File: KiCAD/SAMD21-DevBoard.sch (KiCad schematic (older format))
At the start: 22 parts, among them J1 .1\" Headers, J2 .1\" Headers, J3 Cortex_Debug, SW1 B3FS-4005P, U1 SAMD21G18A-AU, Y1 32.768KHz

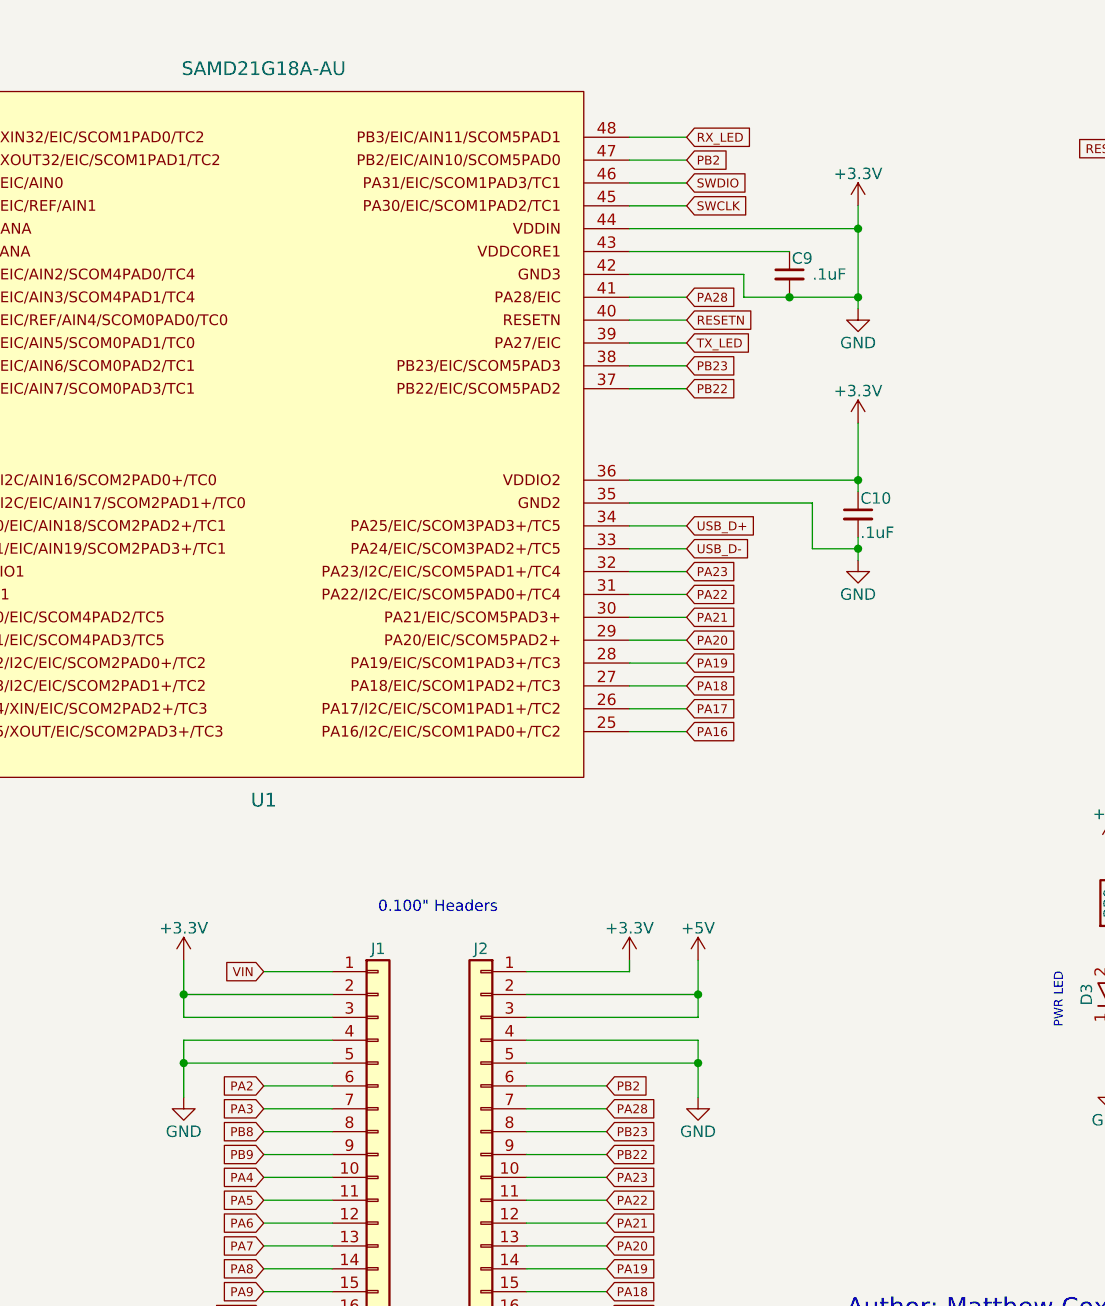
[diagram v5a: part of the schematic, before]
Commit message: Board layout and fixing schematic errors
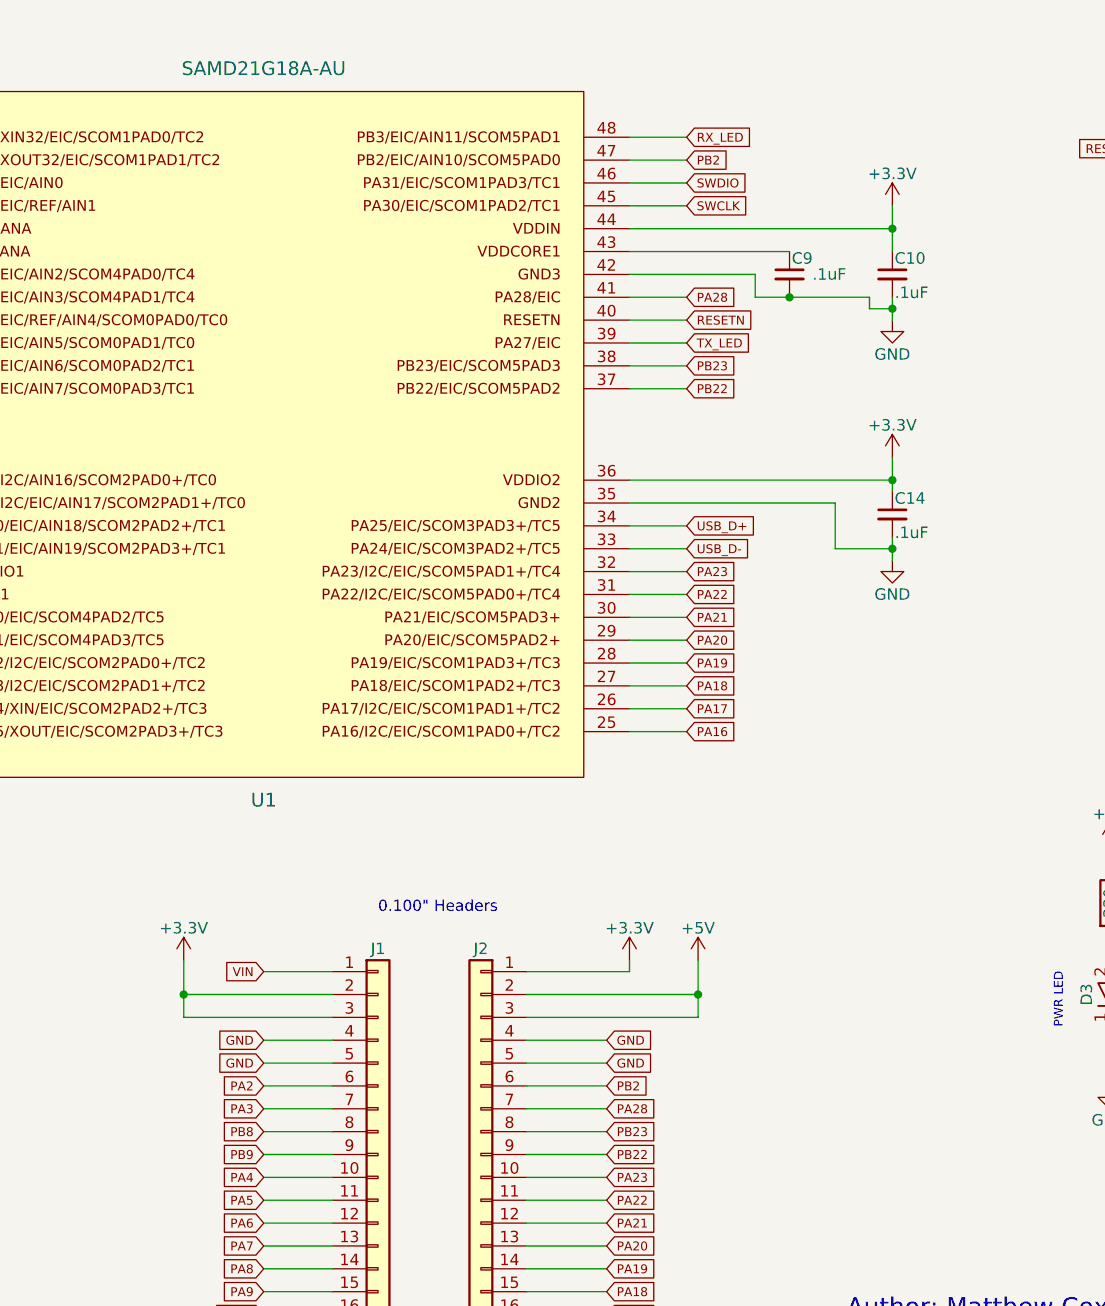
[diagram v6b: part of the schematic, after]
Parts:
- added C14: .1uF, symbol C_Small
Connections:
- net +3V3: now also C14.1; no longer C10.2, C11.2, C12.2, C13.2, C7.1, C8.1, C9.2, D3.1 (K), D4.1 (GND), J1.4 (Pin_4), J1.5 (Pin_5), J2.4 (Pin_4), J2.5 (Pin_5), J3.3 (GND), J3.5 (GND), SW1.3, SW1.4, U1.18, U1.35, U1.42, U1.5
- new net GND: C10.2, C11.2, C12.2, C13.2, C14.2, C7.1, C8.1, C9.2, D3.1 (K), D4.1 (GND), J1.4 (Pin_4), J1.5 (Pin_5), J2.4 (Pin_4), J2.5 (Pin_5), J3.3 (GND), J3.5 (GND), SW1.3, SW1.4, U1.18, U1.35, U1.42, U1.5
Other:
- moved on the sheet: C10
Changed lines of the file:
@@
 L +3.3V #PWR04
 U 1 1 5BF30FCE
-P 7100 2100
-F 0 "#PWR04" H 7100 1950 50  0001 C CNN
-F 1 "+3.3V" H 7100 2240 50  0000 C CNN
-F 2 "" H 7100 2100 50  0001 C CNN
-F 3 "" H 7100 2100 50  0001 C CNN
-	1    7100 2100
-	1    0    0    -1
-$EndComp
-$Comp
-L GND #PWR05
-U 1 1 5BF30FEC
-P 7100 2550
-F 0 "#PWR05" H 7100 2300 50  0001 C CNN
-F 1 "GND" H 7100 2400 50  0000 C CNN
-F 2 "" H 7100 2550 50  0001 C CNN
-F 3 "" H 7100 2550 50  0001 C CNN
-	1    7100 2550
+P 7250 2100
+F 0 "#PWR04" H 7250 1950 50  0001 C CNN
+F 1 "+3.3V" H 7250 2240 50  0000 C CNN
+F 2 "" H 7250 2100 50  0001 C CNN
+F 3 "" H 7250 2100 50  0001 C CNN
+	1    7250 2100
 	1    0    0    -1
 $EndComp
@@
 $EndComp
 $Comp
-L +3.3V #PWR06
+L +3.3V #PWR05
 U 1 1 5BF31404
 P 1900 3450
-F 0 "#PWR06" H 1900 3300 50  0001 C CNN
+F 0 "#PWR05" H 1900 3300 50  0001 C CNN
 F 1 "+3.3V" H 1900 3590 50  0000 C CNN
 F 2 "" H 1900 3450 50  0001 C CNN
@@
 $EndComp
 $Comp
-L GND #PWR07
+L GND #PWR06
 U 1 1 5BF3142B
 P 1900 4050
-F 0 "#PWR07" H 1900 3800 50  0001 C CNN
+F 0 "#PWR06" H 1900 3800 50  0001 C CNN
 F 1 "GND" H 1900 3900 50  0000 C CNN
 F 2 "" H 1900 4050 50  0001 C CNN
@@
 $EndComp
 $Comp
-L +3.3V #PWR08
-U 1 1 5BF318C5
-P 7100 3050
-F 0 "#PWR08" H 7100 2900 50  0001 C CNN
-F 1 "+3.3V" H 7100 3190 50  0000 C CNN
-F 2 "" H 7100 3050 50  0001 C CNN
-F 3 "" H 7100 3050 50  0001 C CNN
-	1    7100 3050
-	1    0    0    -1
-$EndComp
-$Comp
-L GND #PWR09
+L GND #PWR07
 U 1 1 5BF318CB
-P 7100 3650
-F 0 "#PWR09" H 7100 3400 50  0001 C CNN
-F 1 "GND" H 7100 3500 50  0000 C CNN
-F 2 "" H 7100 3650 50  0001 C CNN
-F 3 "" H 7100 3650 50  0001 C CNN
-	1    7100 3650
+P 7250 3650
+F 0 "#PWR07" H 7250 3400 50  0001 C CNN
+F 1 "GND" H 7250 3500 50  0000 C CNN
+F 2 "" H 7250 3650 50  0001 C CNN
+F 3 "" H 7250 3650 50  0001 C CNN
+	1    7250 3650
 	1    0    0    -1
 $EndComp
@@
 L C_Small C10
 U 1 1 5BF318D3
-P 7100 3450
-F 0 "C10" H 7110 3520 50  0000 L CNN
-F 1 ".1uF" H 7110 3370 50  0000 L CNN
-F 2 "Capacitors_SMD:C_1206" H 7100 3450 50  0001 C CNN
-F 3 "" H 7100 3450 50  0001 C CNN
-	1    7100 3450
-	1    0    0    -1
-$EndComp
-$Comp
-L GND #PWR010
+P 7250 2400
+F 0 "C10" H 7260 2470 50  0000 L CNN
+F 1 ".1uF" H 7260 2320 50  0000 L CNN
+F 2 "Capacitors_SMD:C_1206" H 7250 2400 50  0001 C CNN
+F 3 "" H 7250 2400 50  0001 C CNN
+	1    7250 2400
+	1    0    0    -1
+$EndComp
+$Comp
+L GND #PWR08
 U 1 1 5BF31BBB
 P 1850 2750
-F 0 "#PWR010" H 1850 2500 50  0001 C CNN
+F 0 "#PWR08" H 1850 2500 50  0001 C CNN
 F 1 "GND" H 1850 2600 50  0000 C CNN
 F 2 "" H 1850 2750 50  0001 C CNN
@@
 $EndComp
 $Comp
-L +3.3V #PWR011
+L +3.3V #PWR09
 U 1 1 5BF31D4F
 P 1850 1950
-F 0 "#PWR011" H 1850 1800 50  0001 C CNN
+F 0 "#PWR09" H 1850 1800 50  0001 C CNN
 F 1 "+3.3V" H 1850 2090 50  0000 C CNN
 F 2 "" H 1850 1950 50  0001 C CNN
@@
 $EndComp
 $Comp
-L GND #PWR012
+L GND #PWR010
 U 1 1 5BF320EF
 P 2250 2450
-F 0 "#PWR012" H 2250 2200 50  0001 C CNN
+F 0 "#PWR010" H 2250 2200 50  0001 C CNN
 F 1 "GND" H 2250 2300 50  0000 C CNN
 F 2 "" H 2250 2450 50  0001 C CNN
@@
 RESETN
 $Comp
-L +3.3V #PWR013
+L +3.3V #PWR011
 U 1 1 5BF3264F
 P 8550 1400
-F 0 "#PWR013" H 8550 1250 50  0001 C CNN
+F 0 "#PWR011" H 8550 1250 50  0001 C CNN
 F 1 "+3.3V" H 8550 1540 50  0000 C CNN
 F 2 "" H 8550 1400 50  0001 C CNN
@@
 $EndComp
 $Comp
-L GND #PWR014
+L GND #PWR012
 U 1 1 5BF32677
 P 9400 2050
-F 0 "#PWR014" H 9400 1800 50  0001 C CNN
+F 0 "#PWR012" H 9400 1800 50  0001 C CNN
 F 1 "GND" H 9400 1900 50  0000 C CNN
 F 2 "" H 9400 2050 50  0001 C CNN
@@
 RESETN
 $Comp
-L +3.3V #PWR015
+L +3.3V #PWR013
 U 1 1 5BF9AAD9
 P 1400 5900
-F 0 "#PWR015" H 1400 5750 50  0001 C CNN
+F 0 "#PWR013" H 1400 5750 50  0001 C CNN
 F 1 "+3.3V" H 1400 6040 50  0000 C CNN
 F 2 "" H 1400 5900 50  0001 C CNN
@@
 $EndComp
 $Comp
-L GND #PWR016
+L GND #PWR014
 U 1 1 5BF9AB6E
 P 1400 6550
-F 0 "#PWR016" H 1400 6300 50  0001 C CNN
+F 0 "#PWR014" H 1400 6300 50  0001 C CNN
 F 1 "GND" H 1400 6400 50  0000 C CNN
 F 2 "" H 1400 6550 50  0001 C CNN
@@
 PA28
 $Comp
-L +3.3V #PWR017
+L +3.3V #PWR015
 U 1 1 5BF9D0E0
 P 4150 5400
-F 0 "#PWR017" H 4150 5250 50  0001 C CNN
+F 0 "#PWR015" H 4150 5250 50  0001 C CNN
 F 1 "+3.3V" H 4150 5540 50  0000 C CNN
 F 2 "" H 4150 5400 50  0001 C CNN
@@
 $EndComp
 $Comp
-L GND #PWR018
-U 1 1 5BF9D10E
-P 4150 6000
-F 0 "#PWR018" H 4150 5750 50  0001 C CNN
-F 1 "GND" H 4150 5850 50  0000 C CNN
-F 2 "" H 4150 6000 50  0001 C CNN
-F 3 "" H 4150 6000 50  0001 C CNN
-	1    4150 6000
-	1    0    0    -1
-$EndComp
-$Comp
-L +3.3V #PWR019
+L +3.3V #PWR016
 U 1 1 5BF9D13C
 P 6100 5400
-F 0 "#PWR019" H 6100 5250 50  0001 C CNN
+F 0 "#PWR016" H 6100 5250 50  0001 C CNN
 F 1 "+3.3V" H 6100 5540 50  0000 C CNN
 F 2 "" H 6100 5400 50  0001 C CNN
 F 3 "" H 6100 5400 50  0001 C CNN
 	1    6100 5400
-	1    0    0    -1
-$EndComp
-$Comp
-L GND #PWR020
-U 1 1 5BF9D16A
-P 6400 6000
-F 0 "#PWR020" H 6400 5750 50  0001 C CNN
-F 1 "GND" H 6400 5850 50  0000 C CNN
-F 2 "" H 6400 6000 50  0001 C CNN
-F 3 "" H 6400 6000 50  0001 C CNN
-	1    6400 6000
 	1    0    0    -1
 $EndComp
@@
 $EndComp
 $Comp
-L +5V #PWR021
+L +5V #PWR017
 U 1 1 5BF9E687
 P 6400 5400
-F 0 "#PWR021" H 6400 5250 50  0001 C CNN
+F 0 "#PWR017" H 6400 5250 50  0001 C CNN
 F 1 "+5V" H 6400 5540 50  0000 C CNN
 F 2 "" H 6400 5400 50  0001 C CNN
@@
 Connection ~ 2400 1200
 Wire Wire Line
-	6100 2200 7100 2200
-Wire Wire Line
-	7100 2100 7100 2550
-Connection ~ 7100 2200
-Wire Wire Line
 	6100 2300 6800 2300
 Wire Wire Line
-	6600 2500 7100 2500
-Wire Wire Line
-	6100 2400 6600 2400
-Wire Wire Line
-	6600 2400 6600 2500
-Connection ~ 6800 2500
+	6100 2400 6650 2400
 Wire Wire Line
 	1900 3450 1900 3750
-Wire Wire Line
-	1900 3700 2900 3700
 Connection ~ 1900 3700
 Wire Wire Line
@@
 Wire Wire Line
 	2100 4000 1900 4000
-Wire Wire Line
-	7100 3050 7100 3350
-Wire Wire Line
-	7100 3300 6100 3300
-Connection ~ 7100 3300
-Wire Wire Line
-	7100 3550 7100 3650
-Wire Wire Line
-	6100 3400 6900 3400
-Wire Wire Line
-	6900 3400 6900 3600
-Wire Wire Line
-	6900 3600 7100 3600
 Wire Wire Line
 	1850 2050 1850 1950
@@
 	6100 5450 6100 5400
 Wire Wire Line
-	6400 5750 6400 6000
-Wire Wire Line
-	6400 5750 5650 5750
-Wire Wire Line
-	5650 5850 6400 5850
-Connection ~ 6400 5850
-Wire Wire Line
 	5650 5950 6000 5950
 Wire Wire Line
@@
 	4800 5550 4150 5550
 Connection ~ 4150 5550
-Wire Wire Line
-	4150 5750 4150 6000
-Wire Wire Line
-	4150 5750 4800 5750
-Wire Wire Line
-	4800 5850 4150 5850
-Connection ~ 4150 5850
 $Comp
 L B3FS-4005P SW1
@@
 $EndComp
 $Comp
-L GND #PWR022
+L GND #PWR018
 U 1 1 5C02F19A
 P 1450 2750
-F 0 "#PWR022" H 1450 2500 50  0001 C CNN
+F 0 "#PWR018" H 1450 2500 50  0001 C CNN
 F 1 "GND" H 1450 2600 50  0000 C CNN
 F 2 "" H 1450 2750 50  0001 C CNN
@@
 $EndComp
 $Comp
-L +5V #PWR023
+L +5V #PWR019
 U 1 1 5C03F43E
 P 8850 4900
-F 0 "#PWR023" H 8850 4750 50  0001 C CNN
+F 0 "#PWR019" H 8850 4750 50  0001 C CNN
 F 1 "+5V" H 8850 5040 50  0000 C CNN
 F 2 "" H 8850 4900 50  0001 C CNN
@@
 $EndComp
 $Comp
-L +5V #PWR024
+L +5V #PWR020
 U 1 1 5C03F474
 P 9500 4900
-F 0 "#PWR024" H 9500 4750 50  0001 C CNN
+F 0 "#PWR020" H 9500 4750 50  0001 C CNN
 F 1 "+5V" H 9500 5040 50  0000 C CNN
 F 2 "" H 9500 4900 50  0001 C CNN
@@
 $EndComp
 $Comp
-L +5V #PWR025
+L +5V #PWR021
 U 1 1 5C040822
 P 8200 4900
-F 0 "#PWR025" H 8200 4750 50  0001 C CNN
+F 0 "#PWR021" H 8200 4750 50  0001 C CNN
 F 1 "+5V" H 8200 5040 50  0000 C CNN
 F 2 "" H 8200 4900 50  0001 C CNN
@@
 	8200 5950 8200 5700
 $Comp
-L GND #PWR026
+L GND #PWR022
 U 1 1 5C040992
 P 8200 5950
-F 0 "#PWR026" H 8200 5700 50  0001 C CNN
+F 0 "#PWR022" H 8200 5700 50  0001 C CNN
 F 1 "GND" H 8200 5800 50  0000 C CNN
 F 2 "" H 8200 5950 50  0001 C CNN
@@
 Text Notes 1650 5550 0    79   ~ 0
 Note: VCC from external??
-Connection ~ 7100 3600
-Connection ~ 7100 2500
 Connection ~ 1900 4000
 NoConn ~ 2700 6250
@@
 NoConn ~ 1500 6350
 NoConn ~ 1500 6450
+Text GLabel 6000 5750 2    39   Input ~ 0
+GND
+Text GLabel 6000 5850 2    39   Input ~ 0
+GND
+Text GLabel 4500 5750 0    39   Input ~ 0
+GND
+Text GLabel 4500 5850 0    39   Input ~ 0
+GND
+Wire Wire Line
+	4500 5750 4800 5750
+Wire Wire Line
+	4500 5850 4800 5850
+Wire Wire Line
+	5650 5750 6000 5750
+Wire Wire Line
+	5650 5850 6000 5850
+Wire Wire Line
+	6650 2400 6650 2500
+Wire Wire Line
+	7250 2300 7250 2100
+Wire Wire Line
+	6100 2200 7250 2200
+Connection ~ 7250 2200
+$Comp
+L GND #PWR023
+U 1 1 5C0C2A65
+P 7250 2600
+F 0 "#PWR023" H 7250 2350 50  0001 C CNN
+F 1 "GND" H 7250 2450 50  0000 C CNN
+F 2 "" H 7250 2600 50  0001 C CNN
+F 3 "" H 7250 2600 50  0001 C CNN
+	1    7250 2600
+	1    0    0    -1
+$EndComp
+Wire Wire Line
+	7250 2500 7250 2600
+$Comp
+L C_Small C14
+U 1 1 5C0C391A
+P 7250 3450
+F 0 "C14" H 7260 3520 50  0000 L CNN
+F 1 ".1uF" H 7260 3370 50  0000 L CNN
+F 2 "" H 7250 3450 50  0001 C CNN
+F 3 "" H 7250 3450 50  0001 C CNN
+	1    7250 3450
+	1    0    0    -1
+$EndComp
+Wire Wire Line
+	6100 3400 7000 3400
+Wire Wire Line
+	7000 3400 7000 3600
+$Comp
+L +3.3V #PWR024
+U 1 1 5C0C3C34
+P 7250 3200
+F 0 "#PWR024" H 7250 3050 50  0001 C CNN
+F 1 "+3.3V" H 7250 3340 50  0000 C CNN
+F 2 "" H 7250 3200 50  0001 C CNN
+F 3 "" H 7250 3200 50  0001 C CNN
+	1    7250 3200
+	1    0    0    -1
+$EndComp
+Wire Wire Line
+	7250 3200 7250 3350
+Wire Wire Line
+	6100 3300 7250 3300
+Wire Wire Line
+	1900 3700 2900 3700
+Wire Wire Line
+	7250 3550 7250 3650
+Wire Wire Line
+	7000 3600 7250 3600
+Connection ~ 7250 3600
+Connection ~ 7250 3300
+Wire Wire Line
+	6650 2500 7150 2500
+Wire Wire Line
+	7150 2500 7150 2550
+Wire Wire Line
+	7150 2550 7250 2550
+Connection ~ 7250 2550
+Connection ~ 6800 2500
 $EndSCHEMATC

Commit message: Place and route
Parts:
- C14: footprint (none) -> Capacitors_SMD:C_1206
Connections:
- net +3V3: now also R3.1, R4.1, R5.1
- net +5V: no longer R3.1, R4.1, R5.1
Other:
- note removed: "Note: VCC from external??"
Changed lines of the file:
@@
 LIBS:cortex_debug
 LIBS:B3FS-4005P
+LIBS:lm1117_edited
 LIBS:SAMD21-DevBoard-cache
 EELAYER 25 0
@@
 $EndComp
 $Comp
-L +5V #PWR019
-U 1 1 5C03F43E
-P 8850 4900
-F 0 "#PWR019" H 8850 4750 50  0001 C CNN
-F 1 "+5V" H 8850 5040 50  0000 C CNN
-F 2 "" H 8850 4900 50  0001 C CNN
-F 3 "" H 8850 4900 50  0001 C CNN
-	1    8850 4900
-	1    0    0    -1
-$EndComp
-$Comp
-L +5V #PWR020
-U 1 1 5C03F474
-P 9500 4900
-F 0 "#PWR020" H 9500 4750 50  0001 C CNN
-F 1 "+5V" H 9500 5040 50  0000 C CNN
-F 2 "" H 9500 4900 50  0001 C CNN
-F 3 "" H 9500 4900 50  0001 C CNN
-	1    9500 4900
-	1    0    0    -1
-$EndComp
-$Comp
 L LED D2
 U 1 1 5C03F4AA
@@
 $EndComp
 Wire Wire Line
-	8850 5000 8850 4900
-Wire Wire Line
-	9500 5000 9500 4900
+	8850 4800 8850 5000
+Wire Wire Line
+	9500 4800 9500 5000
 Wire Wire Line
 	8850 5400 8850 5300
@@
 $EndComp
 $Comp
-L +5V #PWR021
-U 1 1 5C040822
-P 8200 4900
-F 0 "#PWR021" H 8200 4750 50  0001 C CNN
-F 1 "+5V" H 8200 5040 50  0000 C CNN
-F 2 "" H 8200 4900 50  0001 C CNN
-F 3 "" H 8200 4900 50  0001 C CNN
-	1    8200 4900
-	1    0    0    -1
-$EndComp
-$Comp
 L R R5
 U 1 1 5C040828
@@
 $EndComp
 Wire Wire Line
-	8200 5000 8200 4900
+	8200 4800 8200 5000
 Wire Wire Line
 	8200 5400 8200 5300
@@
 	8200 5950 8200 5700
 $Comp
-L GND #PWR022
+L GND #PWR019
 U 1 1 5C040992
 P 8200 5950
-F 0 "#PWR022" H 8200 5700 50  0001 C CNN
+F 0 "#PWR019" H 8200 5700 50  0001 C CNN
 F 1 "GND" H 8200 5800 50  0000 C CNN
 F 2 "" H 8200 5950 50  0001 C CNN
@@
 Wire Wire Line
 	2700 6050 2900 6050
-Text Notes 1650 5550 0    79   ~ 0
-Note: VCC from external??
 Connection ~ 1900 4000
 NoConn ~ 2700 6250
@@
 Connection ~ 7250 2200
 $Comp
-L GND #PWR023
+L GND #PWR020
 U 1 1 5C0C2A65
 P 7250 2600
-F 0 "#PWR023" H 7250 2350 50  0001 C CNN
+F 0 "#PWR020" H 7250 2350 50  0001 C CNN
 F 1 "GND" H 7250 2450 50  0000 C CNN
 F 2 "" H 7250 2600 50  0001 C CNN
@@
 F 0 "C14" H 7260 3520 50  0000 L CNN
 F 1 ".1uF" H 7260 3370 50  0000 L CNN
-F 2 "" H 7250 3450 50  0001 C CNN
+F 2 "Capacitors_SMD:C_1206" H 7250 3450 50  0001 C CNN
 F 3 "" H 7250 3450 50  0001 C CNN
 	1    7250 3450
@@
 	7000 3400 7000 3600
 $Comp
-L +3.3V #PWR024
+L +3.3V #PWR021
 U 1 1 5C0C3C34
 P 7250 3200
-F 0 "#PWR024" H 7250 3050 50  0001 C CNN
+F 0 "#PWR021" H 7250 3050 50  0001 C CNN
 F 1 "+3.3V" H 7250 3340 50  0000 C CNN
 F 2 "" H 7250 3200 50  0001 C CNN
@@
 Connection ~ 7250 2550
 Connection ~ 6800 2500
+$Comp
+L +3.3V #PWR022
+U 1 1 5C0C790D
+P 8200 4800
+F 0 "#PWR022" H 8200 4650 50  0001 C CNN
+F 1 "+3.3V" H 8200 4940 50  0000 C CNN
+F 2 "" H 8200 4800 50  0001 C CNN
+F 3 "" H 8200 4800 50  0001 C CNN
+	1    8200 4800
+	1    0    0    -1
+$EndComp
+$Comp
+L +3.3V #PWR023
+U 1 1 5C0C794F
+P 8850 4800
+F 0 "#PWR023" H 8850 4650 50  0001 C CNN
+F 1 "+3.3V" H 8850 4940 50  0000 C CNN
+F 2 "" H 8850 4800 50  0001 C CNN
+F 3 "" H 8850 4800 50  0001 C CNN
+	1    8850 4800
+	1    0    0    -1
+$EndComp
+$Comp
+L +3.3V #PWR024
+U 1 1 5C0C7991
+P 9500 4800
+F 0 "#PWR024" H 9500 4650 50  0001 C CNN
+F 1 "+3.3V" H 9500 4940 50  0000 C CNN
+F 2 "" H 9500 4800 50  0001 C CNN
+F 3 "" H 9500 4800 50  0001 C CNN
+	1    9500 4800
+	1    0    0    -1
+$EndComp
 $EndSCHEMATC
